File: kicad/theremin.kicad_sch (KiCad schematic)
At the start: 45 parts, among them J1 Eurorack Mono Jack, J3 Expression Attachment, SW1 SW_SPDT, U1 4069, U2 4069, U3 LM386, U4 LP2950-5.0_TO92

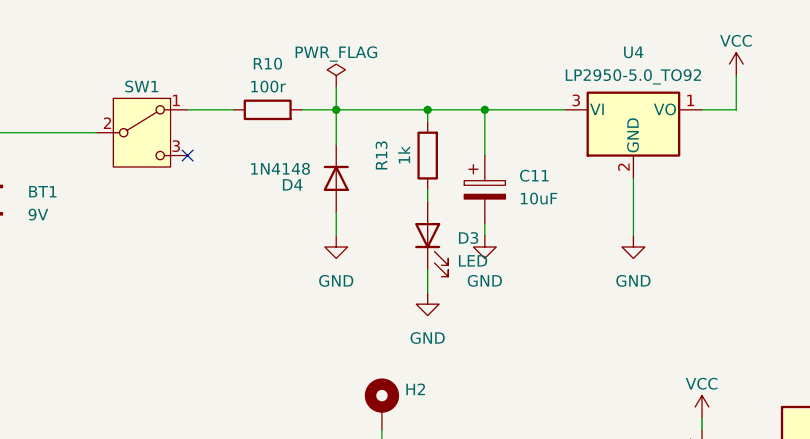
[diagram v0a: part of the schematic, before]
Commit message: Updating correct LED resistor value
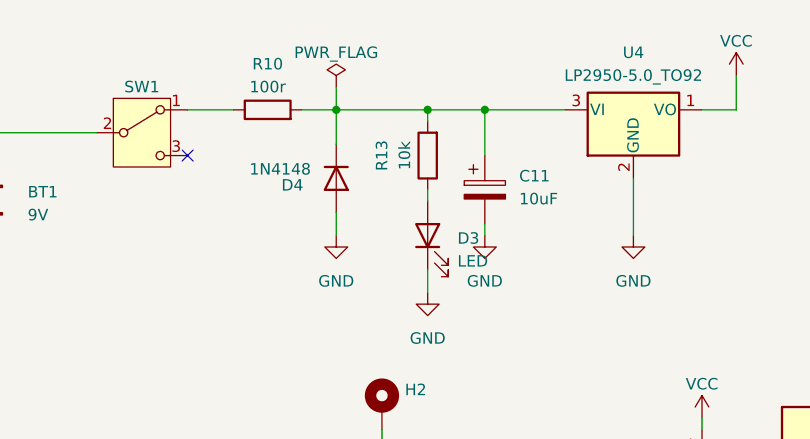
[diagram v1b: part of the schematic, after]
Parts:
- R13: value 1k -> 10k
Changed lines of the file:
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@@
 			)
 		)
-		(property "Value" "1k"
+		(property "Value" "10k"
 			(at 72.39 34.29 90)
 			(effects
